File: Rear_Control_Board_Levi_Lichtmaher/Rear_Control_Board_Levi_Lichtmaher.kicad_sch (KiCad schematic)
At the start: 117 parts, among them J1 430450200, J10 Molex Micro-Fit 4 Pin, J11 22035035, J12 22035035, J13 Conn_01x01_Socket, J14 Conn_01x01_Socket, J2 430450200, J3 430450200, J4 430450200, J5 430450200, J6 430450200, J7 430450200, J8 430450200, J9 22035035, Q1 PSMN1R8-40YLC_115, Q2 PSMN1R8-40YLC_115, Q3 PSMN1R8-40YLC_115, Q4 PSMN1R8-40YLC_115, U11 MCP6286T-E/OT, U12 MCP6286T-E/OT, U2 ADS1118QDGSRQ1, U3 MCP2562-E/P, U4 UA78M05QDCYRG4Q1, U5 ASM330LHHTR, U6 MCP6286T-E/OT

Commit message: ready to order
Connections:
- no-connect marks 47 -> 48
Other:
- moved on the sheet: TP10, TP7, TP9

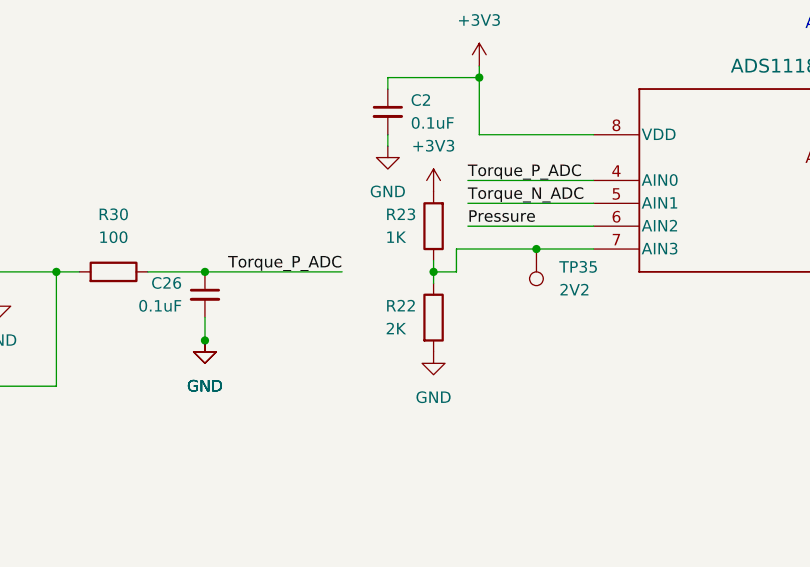
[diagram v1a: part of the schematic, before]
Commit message: changed a few resistor values
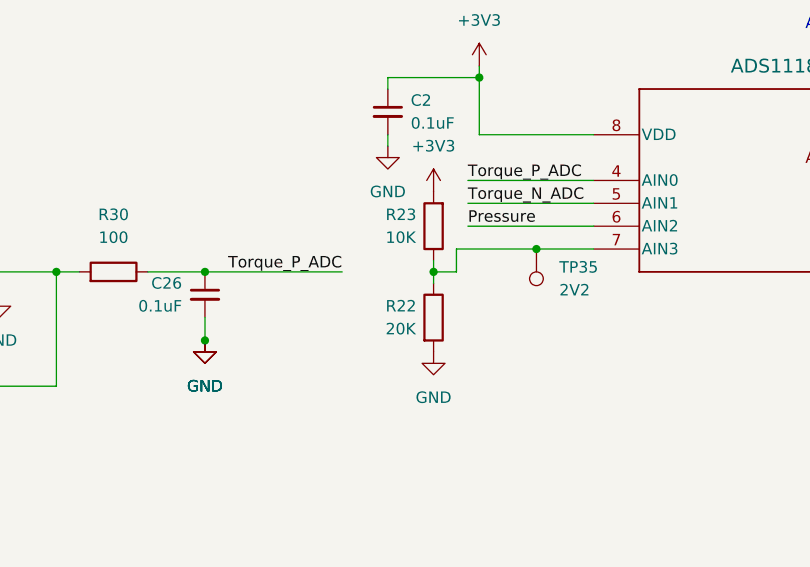
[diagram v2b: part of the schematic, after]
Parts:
- R22: value 2K -> 20K
- R23: value 1K -> 10K
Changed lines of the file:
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@@
 			)
 		)
-		(property "Value" "1K"
+		(property "Value" "10K"
 			(at 218.186 217.17 0)
 			(effects
@@
 			)
 		)
-		(property "Value" "2K"
+		(property "Value" "20K"
 			(at 218.186 227.33 0)
 			(effects

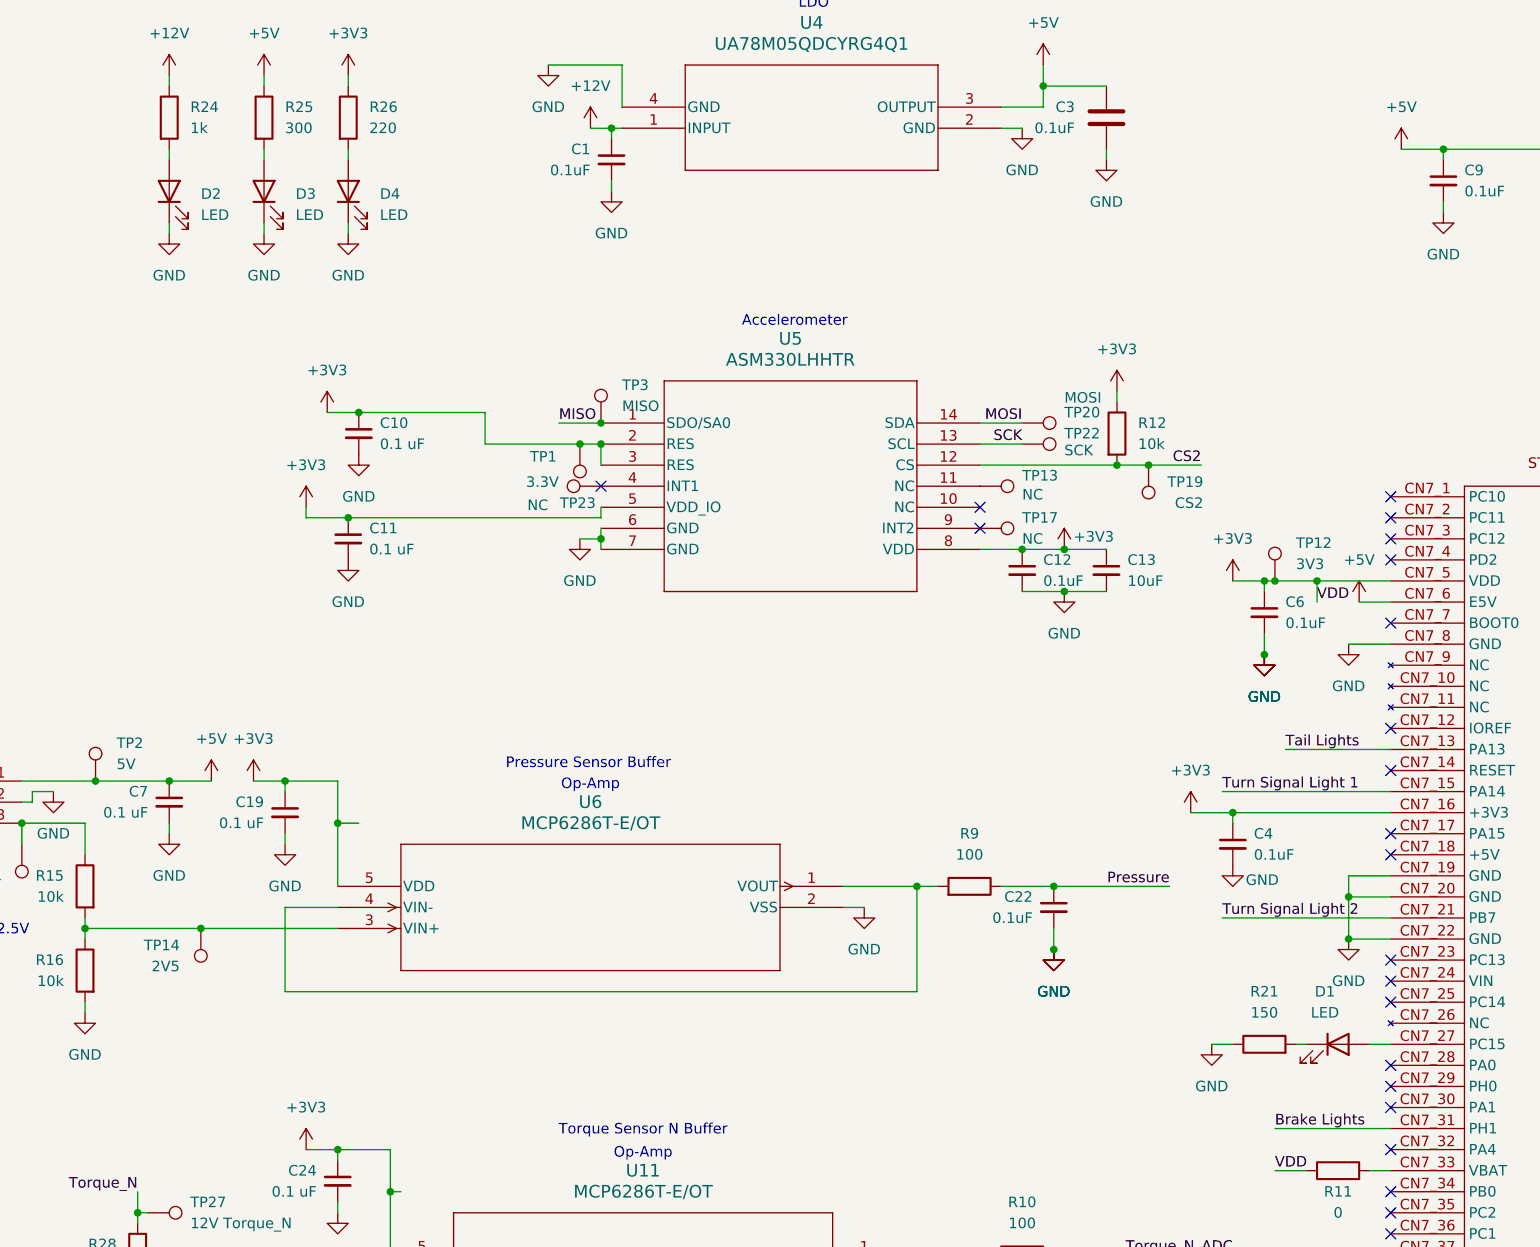
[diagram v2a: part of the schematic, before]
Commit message: changed led footprint
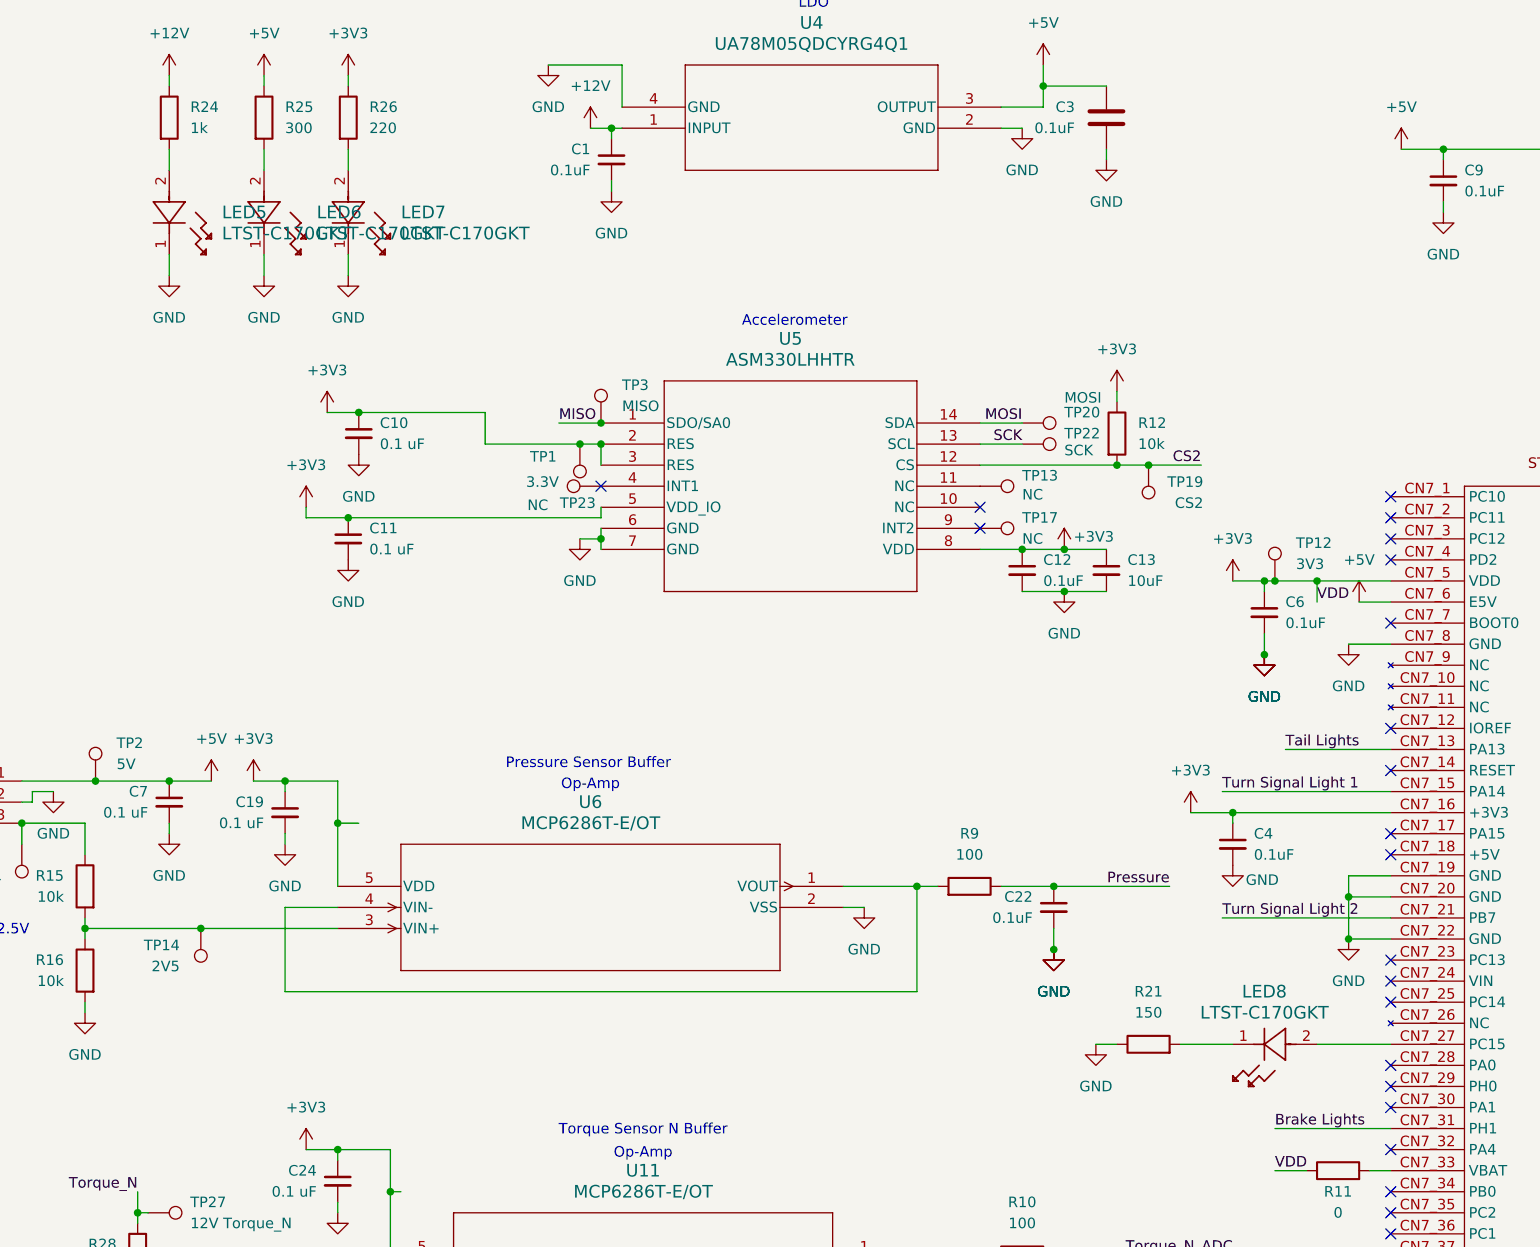
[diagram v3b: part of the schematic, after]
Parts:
- removed D1, D2, D3, D4: LED, SMV_Passives:WL-SMCW_0603(diode), symbol Device:LED
- added LED5, LED6, LED7, LED8: LTST-C170GKT, Personal:LED_LTST-C170GKT_LTO, symbol Green LED:LTST-C170GKT
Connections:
- net GND: now also LED5.1, LED6.1, LED7.1
- net at U7.CN7_27 (PC15): now also LED8.2
- net at R24.2: now also LED5.2
- net at R26.2: now also LED7.2
- net at R21.2: now also LED8.1
- net at R25.2: now also LED6.2
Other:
- moved on the sheet: R21
